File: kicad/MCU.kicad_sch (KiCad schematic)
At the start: 80 parts, among them J10 Display, J7 USART, J8 FAN, J9 USB_A, Q6 NX138AKR, Q7 NX138AKR, Q8 NX138AKR, SW1 RST, SW2 BOOT, SW3 ENC0 (Voltage), SW4 ENC1 (Current), U4 STM32F373C8Tx, U5 USBLC6-2SC6, U6 MCP9700A, Y1 Crystal

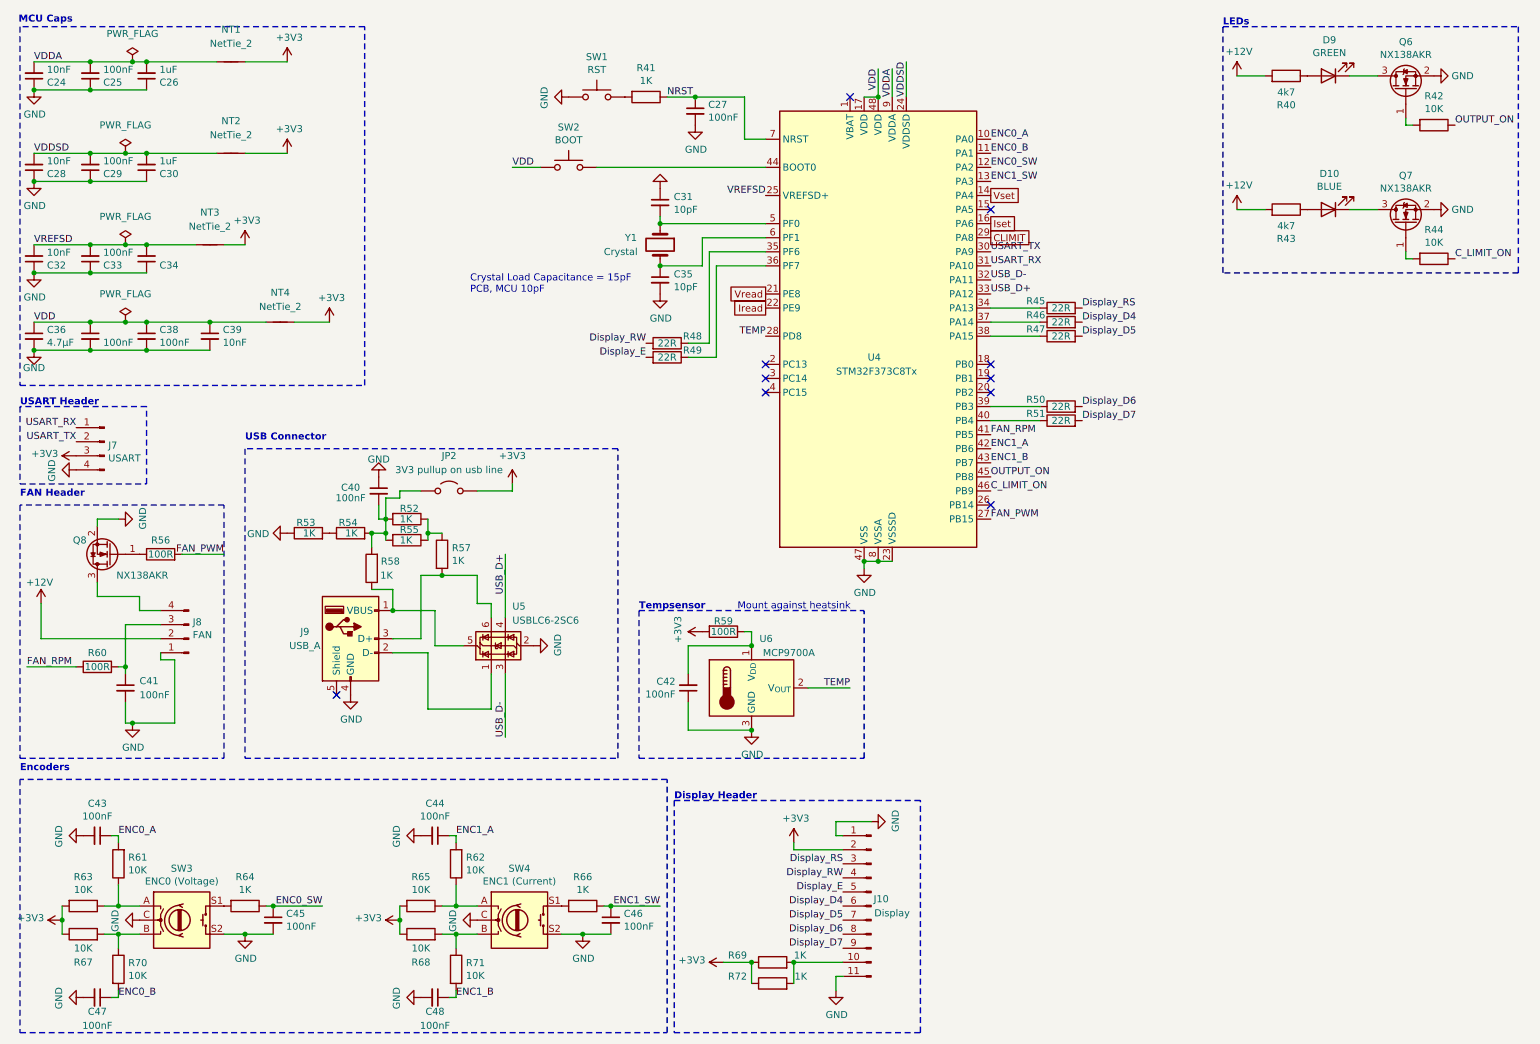
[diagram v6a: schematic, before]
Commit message: Changes
- USB C connector
- 12V Buck converter instead of LM317
- Bunch of stuff I don't remember
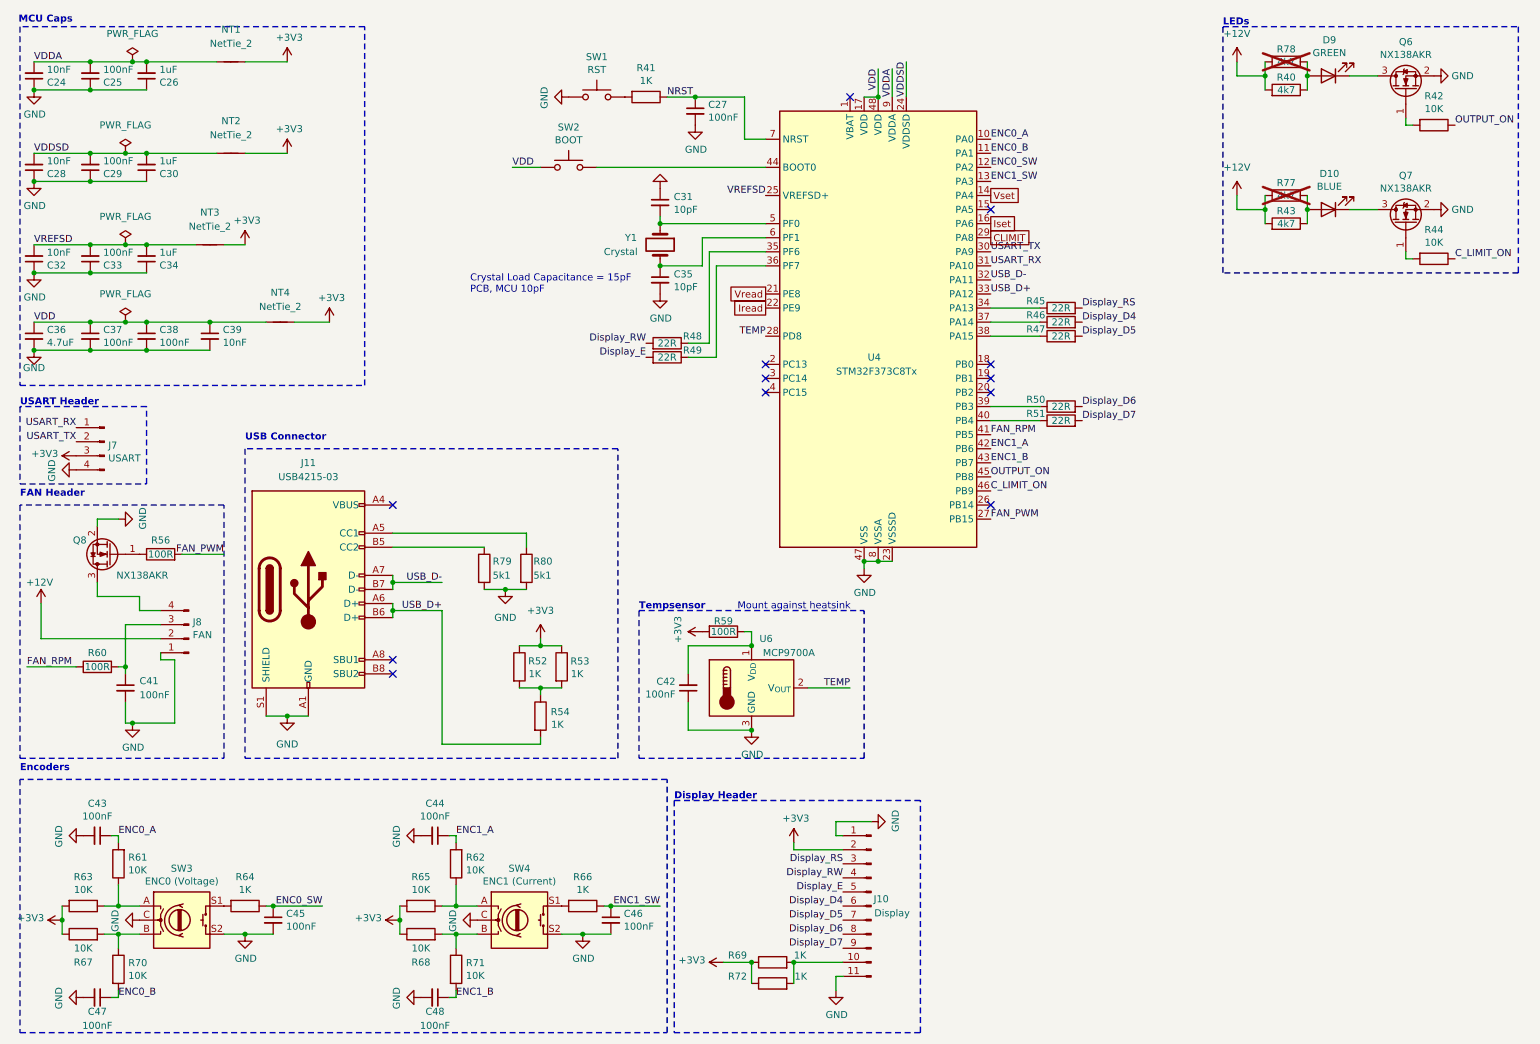
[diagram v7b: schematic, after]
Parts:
- removed C40: 100nF, Capacitor_SMD:C_0805_2012Metric_Pad1.18x1.45mm_HandSolder, symbol Device:C_Small
- removed J9: USB_A, footprints:USBA, symbol Connector:USB_A
- removed JP2: 3V3 pullup on usb line, Jumper:SolderJumper-2_P1.3mm_Open_Pad1.0x1.5mm, symbol Jumper:Jumper_2_Open
- removed R55, R57, R58: 1K, Resistor_SMD:R_0805_2012Metric_Pad1.20x1.40mm_HandSolder, symbol Device:R
- removed U5: USBLC6-2SC6, Package_TO_SOT_SMD:SOT-23-6, symbol Power_Protection:USBLC6-2SC6
- added J11: USB4215-03, footprints:USB_C_Receptacle_GCT_USB4215-xx, symbol Connector:USB_C_Receptacle_USB2.0_16P
- added R77, R78: 4k7, Resistor_SMD:R_0805_2012Metric_Pad1.20x1.40mm_HandSolder, symbol Device:R
- added R79, R80: 5k1, symbol Device:R
- C36: value 4.7µF -> 4.7uF; MPN GRM21BR61H475ME51L -> GRM21BR61H475ME51L
- R41, R52, R53, R54, R64, R66, R69, R72: MPN RT0805FRE071KL -> RC0805FR-131KL
- R42, R44, R61, R62, R63, R65, R67, R68, R70, R71: MPN RC0805FR-1310KL -> RC0805FR-1310KL
- R45, R46, R47, R48, R49, R50, R51: MPN (none) -> RK73H2ATTDD22R0F
- R56, R60: MPN (none) -> RC0805FR-13100RL
- R59: MPN RT0805FRE07100RL -> RC0805FR-13100RL
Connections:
- net +12V: now also R77.2, R78.2
- net +3V3: now also R52.1, R53.1
- net GND: now also J11.A1 (GND), J11.A12 (GND), J11.B1 (GND), J11.B12 (GND), J11.S1 (SHIELD), R79.2, R80.2; no longer R53.1
- net USB_D+: now also R54.2, J11.A6 (D+), J11.B6 (D+)
- net USB_D-: now also J11.A7 (D-), J11.B7 (D-)
- net at D10.2 (A), R43.1: now also R77.1
- net at D9.2 (A), R40.1: now also R78.1
- net at R52.2: now also R53.2, R54.1; no longer R54.2
- new net: J11.A5 (CC1), R80.1
- new net: J11.B5 (CC2), R79.1
- new net: J11.A4 (VBUS), J11.A9 (VBUS), J11.B4 (VBUS), J11.B9 (VBUS)
- no-connect marks 10 -> 12
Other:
- moved on the sheet: R40, R43

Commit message: Commit
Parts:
- NT1, NT2, NT3, NT4: now left out of the parts list
- R79, R80: footprint (none) -> Resistor_SMD:R_0805_2012Metric_Pad1.20x1.40mm_HandSolder; MPN (none) -> RK73H2ATTD5101F
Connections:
- net +3V3: now also J7.4 (Pin_4); no longer J7.3 (Pin_3)
- net GND: now also J7.3 (Pin_3); no longer J7.4 (Pin_4)
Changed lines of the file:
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@@
 	(symbol
 		(lib_id "power:+3V3")
-		(at 24.13 92.71 90)
+		(at 24.13 95.25 90)
 		(unit 1)
 		(exclude_from_sim no)
@@
 		(dnp no)
 		(property "Reference" "#PWR045"
-			(at 27.94 92.71 0)
+			(at 27.94 95.25 0)
 			(effects
 				(font
@@
 		)
 		(property "Value" "+3V3"
-			(at 20.8788 92.329 90)
+			(at 20.8788 94.869 90)
 			(effects
 				(font
@@
 		)
 		(property "Footprint" ""
-			(at 24.13 92.71 0)
+			(at 24.13 95.25 0)
 			(effects
 				(font
@@
 		)
 		(property "Datasheet" ""
-			(at 24.13 92.71 0)
+			(at 24.13 95.25 0)
 			(effects
 				(font
@@
 		)
 		(property "Description" "Power symbol creates a global label with name \"+3V3\""
-			(at 24.13 92.71 0)
+			(at 24.13 95.25 0)
 			(effects
 				(font
@@
 	(symbol
 		(lib_id "power:GND")
-		(at 24.13 95.25 270)
+		(at 24.13 92.71 270)
 		(unit 1)
 		(exclude_from_sim no)
@@
 		(dnp no)
 		(property "Reference" "#PWR046"
-			(at 17.78 95.25 0)
+			(at 17.78 92.71 0)
 			(effects
 				(font
@@
 		)
 		(property "Value" "GND"
-			(at 19.7358 95.377 0)
+			(at 19.05 92.456 90)
 			(effects
 				(font
@@
 		)
 		(property "Footprint" ""
-			(at 24.13 95.25 0)
+			(at 24.13 92.71 0)
 			(effects
 				(font
@@
 		)
 		(property "Datasheet" ""
-			(at 24.13 95.25 0)
+			(at 24.13 92.71 0)
 			(effects
 				(font
@@
 		)
 		(property "Description" "Power symbol creates a global label with name \"GND\" , ground"
-			(at 24.13 95.25 0)
+			(at 24.13 92.71 0)
 			(effects
 				(font
@@
 			)
 		)
-		(property "Footprint" ""
+		(property "Footprint" "Resistor_SMD:R_0805_2012Metric_Pad1.20x1.40mm_HandSolder"
 			(at 103.632 113.03 90)
 			(effects
@@
 			)
 		)
+		(property "MPN" "RK73H2ATTD5101F"
+			(at 105.41 113.03 0)
+			(effects
+				(font
+					(size 1.27 1.27)
+				)
+				(hide yes)
+			)
+		)
 		(pin "1"
 		)
@@
 		(unit 1)
 		(exclude_from_sim no)
-		(in_bom yes)
+		(in_bom no)
 		(on_board yes)
 		(dnp no)
@@
 			)
 		)
-		(property "Footprint" ""
+		(property "Footprint" "Resistor_SMD:R_0805_2012Metric_Pad1.20x1.40mm_HandSolder"
 			(at 96.012 113.03 90)
 			(effects
@@
 			)
 		)
+		(property "MPN" "RK73H2ATTD5101F"
+			(at 97.79 113.03 0)
+			(effects
+				(font
+					(size 1.27 1.27)
+				)
+				(hide yes)
+			)
+		)
 		(pin "1"
 		)
@@
 		(unit 1)
 		(exclude_from_sim no)
-		(in_bom yes)
+		(in_bom no)
 		(on_board yes)
 		(dnp no)
@@
 		(unit 1)
 		(exclude_from_sim no)
-		(in_bom yes)
+		(in_bom no)
 		(on_board yes)
 		(dnp no)
@@
 		(unit 1)
 		(exclude_from_sim no)
-		(in_bom yes)
+		(in_bom no)
 		(on_board yes)
 		(dnp no)
